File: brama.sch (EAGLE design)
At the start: 58 parts, among them IC1 AT90USB162A, J1 AVR_SPI_PRG_6OFFSET_PADS

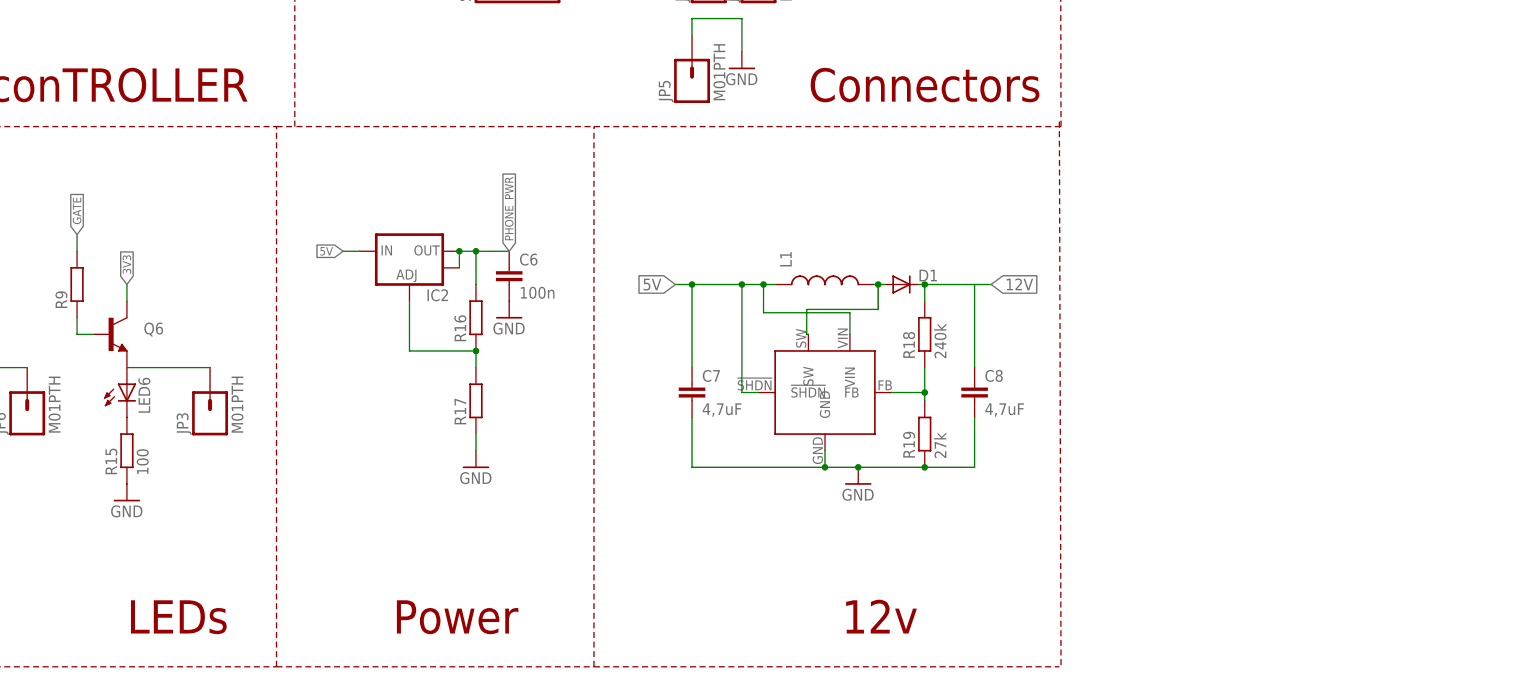
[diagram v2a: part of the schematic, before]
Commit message: L7805 Added
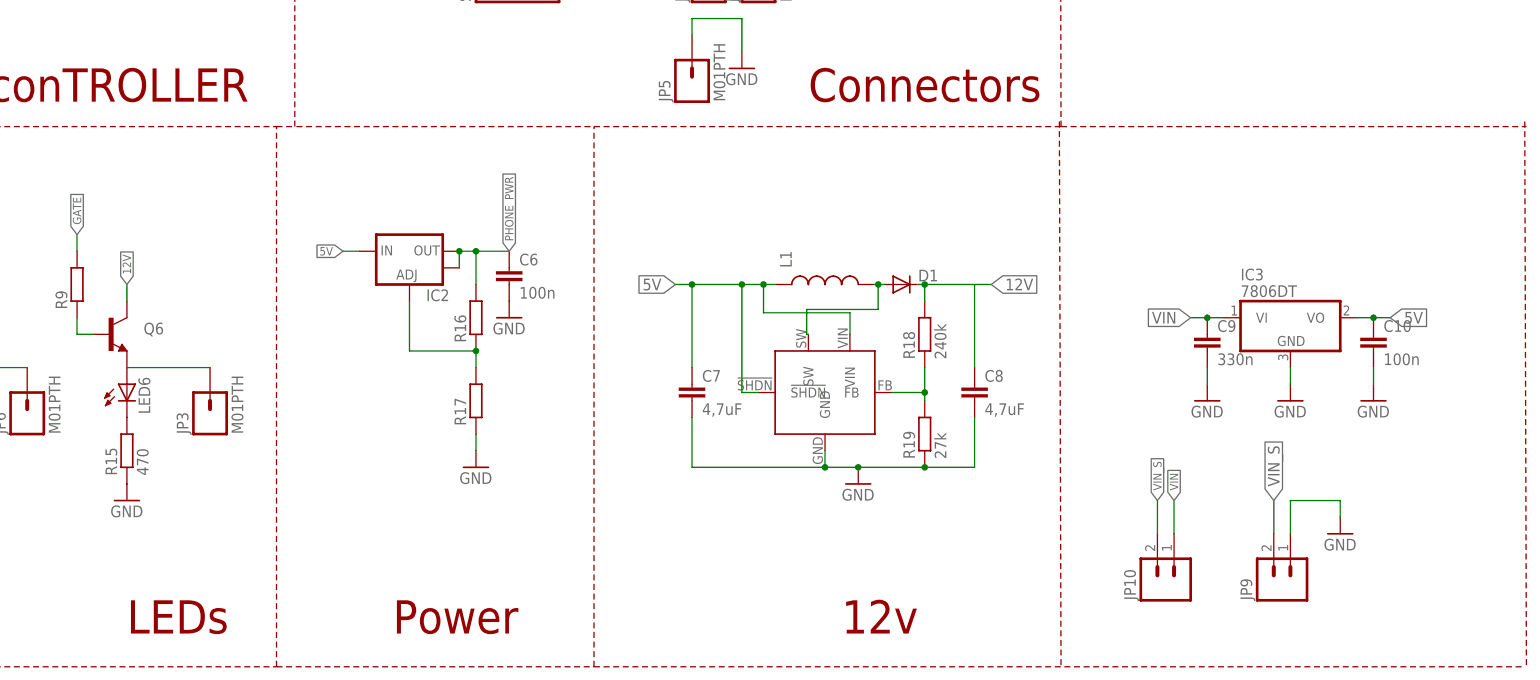
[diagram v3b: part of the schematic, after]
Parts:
- added C10: 100n, rcl:C-EUC0805
- added C9: 330n, rcl:C-EUC0805
- added IC3: 7806DT, linear:7806DT
- added JP10, JP9: (no value), SparkFun-Connectors:M02PTH3
- R15: value 100 -> 470
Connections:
- new net VIN: C9.1, IC3.VI, JP10.1
- new net VIN_S: JP10.2, JP9.2
- net 12V: now also Q6.C
- net 3V3: no longer Q6.C
- net 5V: now also C10.1, IC3.VO
- net GND: now also C10.2, C9.2, IC3.GND, JP9.1
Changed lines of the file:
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@@
 <part name="R13" library="rcl" deviceset="R-EU_" device="R0805" value="100"/>
 <part name="R14" library="rcl" deviceset="R-EU_" device="R0805" value="100"/>
-<part name="R15" library="rcl" deviceset="R-EU_" device="R0805" value="100"/>
+<part name="R15" library="rcl" deviceset="R-EU_" device="R0805" value="470"/>
 <part name="GND4" library="SparkFun-Aesthetics" deviceset="GND" device=""/>
 <part name="GND5" library="SparkFun-Aesthetics" deviceset="GND" device=""/>
@@
 <part name="D1" library="SparkFun-DiscreteSemi" deviceset="DIODE" device="SMB"/>
 <part name="GND18" library="SparkFun-Aesthetics" deviceset="GND" device=""/>
+<part name="IC3" library="linear" deviceset="78*" device="DT" technology="06"/>
+<part name="GND19" library="SparkFun-Aesthetics" deviceset="GND" device=""/>
+<part name="C9" library="rcl" deviceset="C-EU" device="C0805" value="330n"/>
+<part name="C10" library="rcl" deviceset="C-EU" device="C0805" value="100n"/>
+<part name="GND21" library="SparkFun-Aesthetics" deviceset="GND" device=""/>
+<part name="GND22" library="SparkFun-Aesthetics" deviceset="GND" device=""/>
+<part name="JP9" library="SparkFun-Connectors" deviceset="M02" device="PTH3"/>
+<part name="GND23" library="SparkFun-Aesthetics" deviceset="GND" device=""/>
+<part name="JP10" library="SparkFun-Connectors" deviceset="M02" device="PTH3"/>
 </parts>
 <sheets>
@@
 <text x="160.02" y="53.34" size="5.08" layer="94">Power</text>
 <text x="228.6" y="53.34" size="5.08" layer="94">12v</text>
-<wire x1="190.754" y1="48.26" x2="261.874" y2="48.26" width="0.1524" layer="94" style="shortdash"/>
 <wire x1="262.128" y1="48.514" x2="261.874" y2="132.08" width="0.1524" layer="94" style="shortdash"/>
+<wire x1="190.754" y1="48.26" x2="332.994" y2="48.26" width="0.1524" layer="94" style="shortdash"/>
+<wire x1="333.248" y1="48.514" x2="332.994" y2="132.08" width="0.1524" layer="94" style="shortdash"/>
+<wire x1="262.128" y1="130.81" x2="333.248" y2="130.81" width="0.1524" layer="94" style="shortdash"/>
 </plain>
 <instances>
@@
 <instance part="D1" gate="G$1" x="237.744" y="106.68"/>
 <instance part="GND18" gate="1" x="231.14" y="76.2"/>
+<instance part="IC3" gate="A1" x="297.18" y="101.6"/>
+<instance part="GND19" gate="1" x="297.18" y="88.9"/>
+<instance part="C9" gate="G$1" x="284.48" y="99.06"/>
+<instance part="C10" gate="G$1" x="309.88" y="99.06"/>
+<instance part="GND21" gate="1" x="284.48" y="88.9"/>
+<instance part="GND22" gate="1" x="309.88" y="88.9"/>
+<instance part="JP9" gate="G$1" x="297.18" y="60.96" rot="R90"/>
+<instance part="GND23" gate="1" x="304.8" y="68.58"/>
+<instance part="JP10" gate="G$1" x="279.4" y="60.96" rot="R90"/>
 </instances>
 <busses>
@@
 <wire x1="93.98" y1="104.14" x2="93.98" y2="106.68" width="0.1524" layer="91"/>
 <label x="93.98" y="106.68" size="1.27" layer="95" rot="R90" xref="yes"/>
-</segment>
-<segment>
-<pinref part="Q6" gate="G$1" pin="C"/>
-<wire x1="119.38" y1="104.14" x2="119.38" y2="106.68" width="0.1524" layer="91"/>
-<label x="119.38" y="106.68" size="1.27" layer="95" rot="R90" xref="yes"/>
 </segment>
 </net>
@@
 <pinref part="GND18" gate="1" pin="GND"/>
 <junction x="231.14" y="78.74"/>
+</segment>
+<segment>
+<pinref part="IC3" gate="A1" pin="GND"/>
+<pinref part="GND19" gate="1" pin="GND"/>
+<wire x1="297.18" y1="91.44" x2="297.18" y2="93.98" width="0.1524" layer="91"/>
+</segment>
+<segment>
+<pinref part="C9" gate="G$1" pin="2"/>
+<pinref part="GND21" gate="1" pin="GND"/>
+<wire x1="284.48" y1="91.44" x2="284.48" y2="93.98" width="0.1524" layer="91"/>
+</segment>
+<segment>
+<pinref part="C10" gate="G$1" pin="2"/>
+<pinref part="GND22" gate="1" pin="GND"/>
+<wire x1="309.88" y1="91.44" x2="309.88" y2="93.98" width="0.1524" layer="91"/>
+</segment>
+<segment>
+<pinref part="JP9" gate="G$1" pin="1"/>
+<wire x1="297.18" y1="68.58" x2="297.18" y2="73.66" width="0.1524" layer="91"/>
+<wire x1="297.18" y1="73.66" x2="304.8" y2="73.66" width="0.1524" layer="91"/>
+<wire x1="304.8" y1="73.66" x2="304.8" y2="71.12" width="0.1524" layer="91"/>
+<pinref part="GND23" gate="1" pin="GND"/>
 </segment>
 </net>
@@
 <junction x="216.662" y="106.68"/>
 </segment>
+<segment>
+<pinref part="IC3" gate="A1" pin="VO"/>
+<wire x1="307.34" y1="101.6" x2="309.88" y2="101.6" width="0.1524" layer="91"/>
+<label x="312.42" y="101.6" size="1.778" layer="95" xref="yes"/>
+<pinref part="C10" gate="G$1" pin="1"/>
+<wire x1="309.88" y1="101.6" x2="312.42" y2="101.6" width="0.1524" layer="91"/>
+<junction x="309.88" y="101.6"/>
+</segment>
 </net>
 <net name="RESET" class="0">
@@
 <label x="251.46" y="106.68" size="1.778" layer="95" xref="yes"/>
 </segment>
+<segment>
+<pinref part="Q6" gate="G$1" pin="C"/>
+<wire x1="119.38" y1="104.14" x2="119.38" y2="106.68" width="0.1524" layer="91"/>
+<label x="119.38" y="106.68" size="1.27" layer="95" rot="R90" xref="yes"/>
+</segment>
 </net>
 <net name="N$34" class="0">
@@
 </segment>
 </net>
+<net name="VIN" class="0">
+<segment>
+<pinref part="IC3" gate="A1" pin="VI"/>
+<wire x1="287.02" y1="101.6" x2="284.48" y2="101.6" width="0.1524" layer="91"/>
+<label x="281.94" y="101.6" size="1.778" layer="95" rot="R180" xref="yes"/>
+<pinref part="C9" gate="G$1" pin="1"/>
+<wire x1="284.48" y1="101.6" x2="281.94" y2="101.6" width="0.1524" layer="91"/>
+<junction x="284.48" y="101.6"/>
+</segment>
+<segment>
+<pinref part="JP10" gate="G$1" pin="1"/>
+<wire x1="279.4" y1="68.58" x2="279.4" y2="73.66" width="0.1524" layer="91"/>
+<label x="279.4" y="73.66" size="1.27" layer="95" rot="R90" xref="yes"/>
+</segment>
+</net>
+<net name="VIN_S" class="0">
+<segment>
+<pinref part="JP9" gate="G$1" pin="2"/>
+<wire x1="294.64" y1="68.58" x2="294.64" y2="73.66" width="0.1524" layer="91"/>
+<label x="294.64" y="73.66" size="1.778" layer="95" rot="R90" xref="yes"/>
+</segment>
+<segment>
+<pinref part="JP10" gate="G$1" pin="2"/>
+<wire x1="276.86" y1="68.58" x2="276.86" y2="73.66" width="0.1524" layer="91"/>
+<label x="276.86" y="73.66" size="1.27" layer="95" rot="R90" xref="yes"/>
+</segment>
+</net>

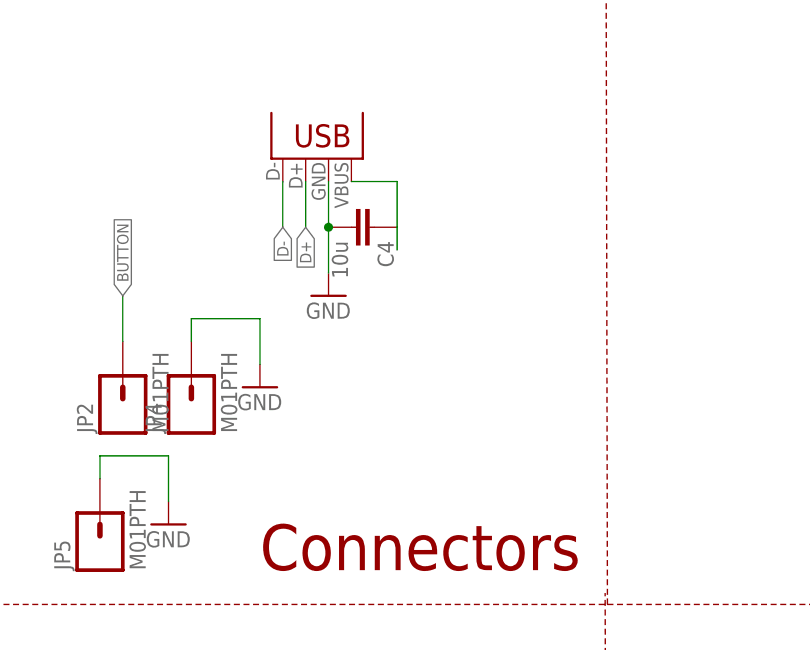
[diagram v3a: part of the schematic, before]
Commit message: USB socket Change
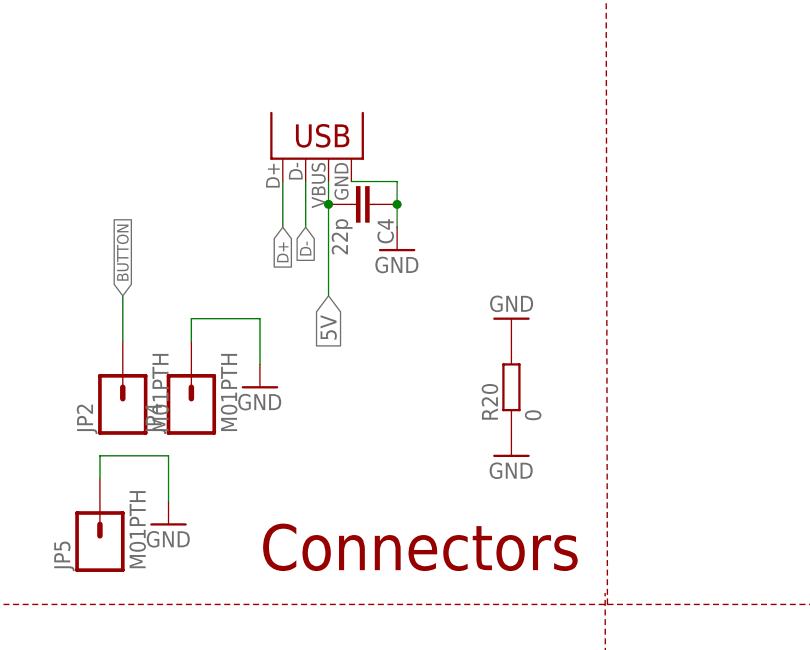
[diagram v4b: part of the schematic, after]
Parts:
- added R20: 0, rcl:R-EU_R0805
- C4: value 10u -> 22p
- JP1: value USB-A-H -> USBSMD; device SparkFun-Connectors:USB-A-H -> SparkFun-Connectors:USBSMD
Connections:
- net 5V: now also C4.2, JP1.VBUS; no longer C4.1, JP1.GND
- net D+: now also JP1.D+; no longer JP1.D-
- net D-: now also JP1.D-; no longer JP1.D+
- net GND: now also C4.1, JP1.GND, R20.1, R20.2; no longer C4.2, JP1.VBUS
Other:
- moved on the sheet: C4
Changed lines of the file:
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@@
 <part name="R1" library="rcl" deviceset="R-EU_" device="R0805" value="22R"/>
 <part name="R2" library="rcl" deviceset="R-EU_" device="R0805" value="22R"/>
-<part name="JP1" library="SparkFun-Connectors" deviceset="USB" device="-A-H" value="USB-A-H"/>
+<part name="JP1" library="SparkFun-Connectors" deviceset="USB" device="SMD" value="USBSMD"/>
 <part name="C1" library="rcl" deviceset="C-EU" device="C0805" value="1uF"/>
 <part name="GND1" library="SparkFun-Aesthetics" deviceset="GND" device=""/>
@@
 <part name="C2" library="rcl" deviceset="C-EU" device="C0805" value="22p"/>
 <part name="C3" library="rcl" deviceset="C-EU" device="C0805" value="22p"/>
-<part name="C4" library="rcl" deviceset="C-EU" device="C0805" value="10u"/>
 <part name="LED1" library="led" deviceset="LED" device="CHIPLED_0805"/>
 <part name="LED2" library="led" deviceset="LED" device="CHIPLED_0805"/>
@@
 <part name="GND14" library="SparkFun-Aesthetics" deviceset="GND" device=""/>
 <part name="FRAME1" library="frames" deviceset="A3L-LOC" device=""/>
-<part name="GND3" library="SparkFun-Aesthetics" deviceset="GND" device=""/>
 <part name="GND15" library="SparkFun-Aesthetics" deviceset="GND" device=""/>
 <part name="JP2" library="SparkFun-Connectors" deviceset="M01" device="PTH"/>
@@
 <part name="GND23" library="SparkFun-Aesthetics" deviceset="GND" device=""/>
 <part name="JP10" library="SparkFun-Connectors" deviceset="M02" device="PTH3"/>
+<part name="GND3" library="SparkFun-Aesthetics" deviceset="GND" device=""/>
+<part name="C4" library="rcl" deviceset="C-EU" device="C0805" value="22p"/>
+<part name="R20" library="rcl" deviceset="R-EU_" device="R0805" value="0"/>
+<part name="GND24" library="SparkFun-Aesthetics" deviceset="GND" device=""/>
+<part name="GND25" library="SparkFun-Aesthetics" deviceset="GND" device=""/>
 </parts>
 <sheets>
@@
 <instance part="C2" gate="G$1" x="50.8" y="193.04" rot="R270"/>
 <instance part="C3" gate="G$1" x="50.8" y="185.42" rot="R270"/>
-<instance part="C4" gate="G$1" x="236.22" y="172.72" rot="R270"/>
 <instance part="LED1" gate="G$1" x="20.32" y="91.44"/>
 <instance part="LED2" gate="G$1" x="33.02" y="91.44"/>
@@
 <instance part="GND14" gate="1" x="177.8" y="101.6"/>
 <instance part="FRAME1" gate="G$1" x="0" y="0"/>
-<instance part="GND3" gate="1" x="231.14" y="165.1"/>
 <instance part="GND15" gate="1" x="121.92" y="170.18"/>
 <instance part="JP2" gate="G$1" x="208.28" y="152.4" rot="R90"/>
@@
 <instance part="GND23" gate="1" x="304.8" y="68.58"/>
 <instance part="JP10" gate="G$1" x="279.4" y="60.96" rot="R90"/>
+<instance part="GND3" gate="1" x="238.76" y="170.18"/>
+<instance part="C4" gate="G$1" x="236.22" y="175.26" rot="R270"/>
+<instance part="R20" gate="G$1" x="251.46" y="154.94" rot="R90"/>
+<instance part="GND24" gate="1" x="251.46" y="147.32"/>
+<instance part="GND25" gate="1" x="251.46" y="162.56" rot="R180"/>
 </instances>
 <busses>
@@
 </segment>
 <segment>
+<pinref part="JP1" gate="G$1" pin="D-"/>
+<wire x1="228.6" y1="177.8" x2="228.6" y2="172.72" width="0.1524" layer="91"/>
+<label x="228.6" y="172.72" size="1.27" layer="95" rot="R270" xref="yes"/>
+</segment>
+</net>
+<net name="D+" class="0">
+<segment>
+<pinref part="R2" gate="G$1" pin="1"/>
+<wire x1="48.26" y1="208.28" x2="45.72" y2="208.28" width="0.1524" layer="91"/>
+<label x="45.72" y="208.28" size="1.27" layer="95" rot="R180" xref="yes"/>
+</segment>
+<segment>
 <pinref part="JP1" gate="G$1" pin="D+"/>
 <wire x1="226.06" y1="177.8" x2="226.06" y2="172.72" width="0.1524" layer="91"/>
 <label x="226.06" y="172.72" size="1.27" layer="95" rot="R270" xref="yes"/>
-</segment>
-</net>
-<net name="D+" class="0">
-<segment>
-<pinref part="R2" gate="G$1" pin="1"/>
-<wire x1="48.26" y1="208.28" x2="45.72" y2="208.28" width="0.1524" layer="91"/>
-<label x="45.72" y="208.28" size="1.27" layer="95" rot="R180" xref="yes"/>
-</segment>
-<segment>
-<pinref part="JP1" gate="G$1" pin="D-"/>
-<wire x1="228.6" y1="177.8" x2="228.6" y2="172.72" width="0.1524" layer="91"/>
-<label x="228.6" y="172.72" size="1.27" layer="95" rot="R270" xref="yes"/>
 </segment>
 </net>
@@
 <pinref part="C6" gate="G$1" pin="2"/>
 <pinref part="GND14" gate="1" pin="GND"/>
-</segment>
-<segment>
-<pinref part="JP1" gate="G$1" pin="VBUS"/>
-<wire x1="231.14" y1="177.8" x2="231.14" y2="172.72" width="0.1524" layer="91"/>
-<pinref part="C4" gate="G$1" pin="2"/>
-<wire x1="231.14" y1="172.72" x2="231.14" y2="167.64" width="0.1524" layer="91"/>
-<junction x="231.14" y="172.72"/>
-<pinref part="GND3" gate="1" pin="GND"/>
 </segment>
 <segment>
@@
 <pinref part="GND23" gate="1" pin="GND"/>
 </segment>
+<segment>
+<pinref part="JP1" gate="G$1" pin="GND"/>
+<wire x1="233.68" y1="177.8" x2="238.76" y2="177.8" width="0.1524" layer="91"/>
+<wire x1="238.76" y1="177.8" x2="238.76" y2="175.26" width="0.1524" layer="91"/>
+<pinref part="GND3" gate="1" pin="GND"/>
+<pinref part="C4" gate="G$1" pin="1"/>
+<wire x1="238.76" y1="175.26" x2="238.76" y2="172.72" width="0.1524" layer="91"/>
+<junction x="238.76" y="175.26"/>
+</segment>
+<segment>
+<pinref part="R20" gate="G$1" pin="1"/>
+<pinref part="GND24" gate="1" pin="GND"/>
+</segment>
+<segment>
+<pinref part="R20" gate="G$1" pin="2"/>
+<pinref part="GND25" gate="1" pin="GND"/>
+</segment>
 </net>
 <net name="5V" class="0">
@@
 <wire x1="154.94" y1="111.76" x2="152.4" y2="111.76" width="0.1524" layer="91"/>
 <label x="152.4" y="111.76" size="1.27" layer="95" rot="R180" xref="yes"/>
-</segment>
-<segment>
-<pinref part="JP1" gate="G$1" pin="GND"/>
-<wire x1="233.68" y1="177.8" x2="238.76" y2="177.8" width="0.1524" layer="91"/>
-<wire x1="238.76" y1="177.8" x2="238.76" y2="172.72" width="0.1524" layer="91"/>
-<pinref part="C4" gate="G$1" pin="1"/>
-<wire x1="238.76" y1="172.72" x2="238.76" y2="170.18" width="0.1524" layer="91"/>
 </segment>
 <segment>
@@
 <junction x="309.88" y="101.6"/>
 </segment>
-</net>
+<segment>
+<pinref part="JP1" gate="G$1" pin="VBUS"/>
+<wire x1="231.14" y1="177.8" x2="231.14" y2="175.26" width="0.1524" layer="91"/>
+<label x="231.14" y="165.1" size="1.778" layer="95" rot="R270" xref="yes"/>
+<pinref part="C4" gate="G$1" pin="2"/>
+<wire x1="231.14" y1="175.26" x2="231.14" y2="165.1" width="0.1524" layer="91"/>
+<junction x="231.14" y="175.26"/>
+</segment>
+</net>
